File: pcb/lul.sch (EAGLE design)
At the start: 86 parts, among them IC1 STM32F072C8T6, IC2 REG1117, IC3 74AHCT1G08DBV, U1 UG-2864HSWEG01

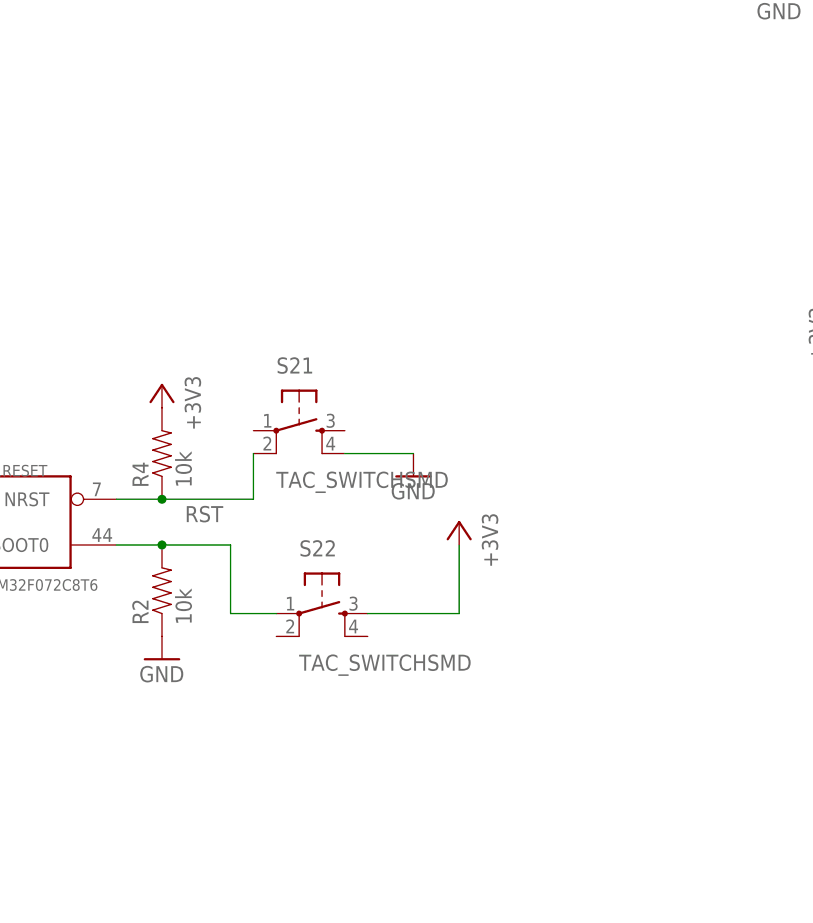
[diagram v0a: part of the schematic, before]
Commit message: replaced DFU and RST button
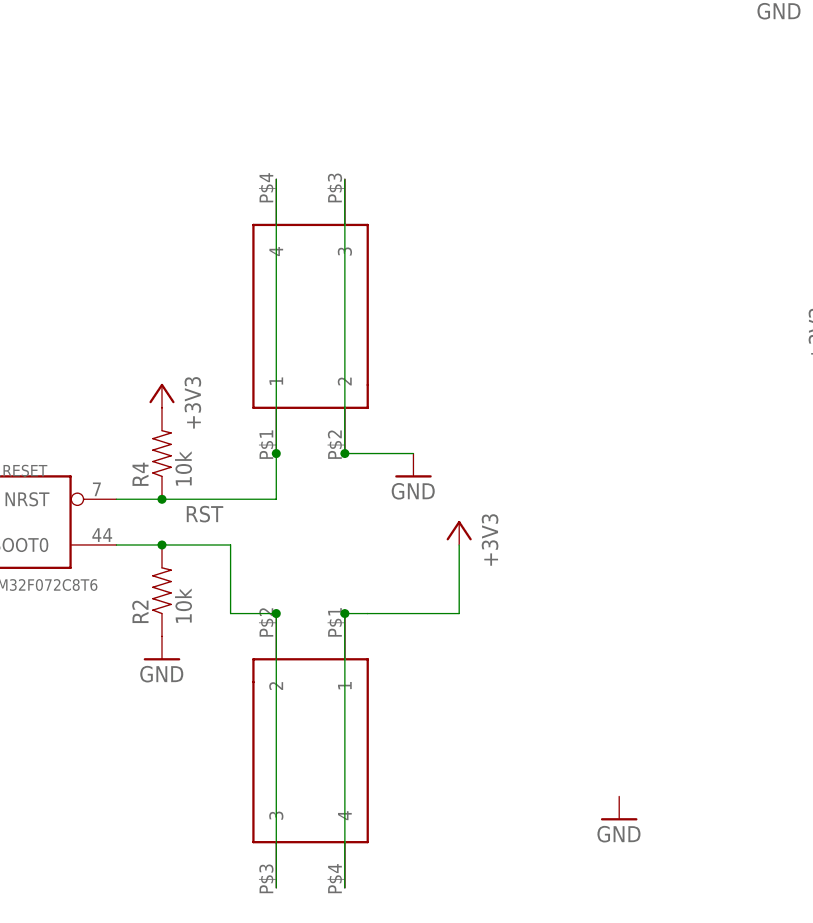
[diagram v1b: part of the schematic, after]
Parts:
- removed S21, S22: TAC_SWITCHSMD, clock:TAC_SWITCHSMD
- added SW1, SW2: 324_SW324_SWITCH_FOOT_HOLE, 3pos_slide_switch:324_SW324_SWITCH_FOOT_HOLE
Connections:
- net +3V3: now also SW1.1, SW1.4; no longer S22.3
- net GND: now also SW2.2, SW2.3; no longer S21.4
- net N$2: now also SW1.2, SW1.3; no longer S22.1
- net RST: now also SW2.1, SW2.4; no longer S21.2
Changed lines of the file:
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@@
 <part name="S19" library="clock" deviceset="TAC_SWITCH" device="SMD" value="TAC_SWITCHSMD"/>
 <part name="S20" library="clock" deviceset="TAC_SWITCH" device="SMD" value="TAC_SWITCHSMD"/>
-<part name="S21" library="clock" deviceset="TAC_SWITCH" device="SMD" value="TAC_SWITCHSMD"/>
-<part name="S22" library="clock" deviceset="TAC_SWITCH" device="SMD" value="TAC_SWITCHSMD"/>
 <part name="IC2" library="clock" deviceset="REG1117" device=""/>
 <part name="+3V3" library="supply1" library_urn="urn:adsk.eagle:library:371" deviceset="+3V3" device=""/>
@@
 <part name="C26" library="clock" deviceset="C-US" device="C1210" value="47uF"/>
 <part name="GND5" library="supply1" library_urn="urn:adsk.eagle:library:371" deviceset="GND" device=""/>
+<part name="GND8" library="supply1" library_urn="urn:adsk.eagle:library:371" deviceset="GND" device=""/>
+<part name="SW2" library="3pos_slide_switch" deviceset="324_SW" device="324_SWITCH_FOOT_HOLE" value="324_SW324_SWITCH_FOOT_HOLE"/>
+<part name="SW1" library="3pos_slide_switch" deviceset="324_SW" device="324_SWITCH_FOOT_HOLE" value="324_SW324_SWITCH_FOOT_HOLE"/>
 </parts>
 <sheets>
@@
 <instance part="S19" gate="S" x="144.78" y="-170.18"/>
 <instance part="S20" gate="S" x="144.78" y="-193.04"/>
-<instance part="S21" gate="S" x="241.3" y="-170.18"/>
-<instance part="S22" gate="S" x="243.84" y="-190.5"/>
 <instance part="IC2" gate="G$1" x="109.22" y="-144.78"/>
 <instance part="+3V3" gate="G$1" x="353.06" y="76.2"/>
@@
 <instance part="C26" gate="G$1" x="86.36" y="-147.32"/>
 <instance part="GND5" gate="1" x="86.36" y="-154.94"/>
+<instance part="GND8" gate="1" x="276.86" y="-213.36"/>
+<instance part="SW2" gate="G$1" x="241.3" y="-157.48" rot="MR90"/>
+<instance part="SW1" gate="G$1" x="243.84" y="-205.74" rot="MR270"/>
 </instances>
 <busses>
@@
 <wire x1="337.82" y1="-180.34" x2="322.58" y2="-180.34" width="0.1524" layer="91"/>
 <junction x="322.58" y="-180.34"/>
-</segment>
-<segment>
-<pinref part="S21" gate="S" pin="4"/>
-<pinref part="GND10" gate="1" pin="GND"/>
-<wire x1="246.38" y1="-172.72" x2="254" y2="-172.72" width="0.1524" layer="91"/>
 </segment>
 <segment>
@@
 <pinref part="GND5" gate="1" pin="GND"/>
 </segment>
+<segment>
+<pinref part="SW2" gate="G$1" pin="2"/>
+<pinref part="GND10" gate="1" pin="GND"/>
+<wire x1="246.38" y1="-172.72" x2="254" y2="-172.72" width="0.1524" layer="91"/>
+<pinref part="SW2" gate="G$1" pin="3"/>
+<wire x1="246.38" y1="-142.24" x2="246.38" y2="-172.72" width="0.1524" layer="91"/>
+<junction x="246.38" y="-172.72"/>
+</segment>
 </net>
 <net name="SCL" class="0">
@@
 </segment>
 <segment>
-<pinref part="S22" gate="S" pin="3"/>
 <pinref part="+3V7" gate="G$1" pin="+3V3"/>
 <wire x1="248.92" y1="-190.5" x2="259.08" y2="-190.5" width="0.1524" layer="91"/>
 <wire x1="259.08" y1="-190.5" x2="259.08" y2="-182.88" width="0.1524" layer="91"/>
+<pinref part="SW1" gate="G$1" pin="1"/>
+<wire x1="248.92" y1="-190.5" x2="246.38" y2="-190.5" width="0.1524" layer="91"/>
+<pinref part="SW1" gate="G$1" pin="4"/>
+<wire x1="246.38" y1="-190.5" x2="246.38" y2="-220.98" width="0.1524" layer="91"/>
+<junction x="246.38" y="-190.5"/>
 </segment>
 <segment>
@@
 <wire x1="233.68" y1="-182.88" x2="233.68" y2="-190.5" width="0.1524" layer="91"/>
 <junction x="226.06" y="-182.88"/>
-<pinref part="S22" gate="S" pin="1"/>
 <wire x1="233.68" y1="-190.5" x2="238.76" y2="-190.5" width="0.1524" layer="91"/>
+<pinref part="SW1" gate="G$1" pin="2"/>
+<pinref part="SW1" gate="G$1" pin="3"/>
+<wire x1="238.76" y1="-190.5" x2="238.76" y2="-220.98" width="0.1524" layer="91"/>
+<junction x="238.76" y="-190.5"/>
 </segment>
 </net>
@@
 <pinref part="R4" gate="G$1" pin="1"/>
 <wire x1="220.98" y1="-177.8" x2="226.06" y2="-177.8" width="0.1524" layer="91"/>
-<pinref part="S21" gate="S" pin="2"/>
-<wire x1="226.06" y1="-177.8" x2="236.22" y2="-177.8" width="0.1524" layer="91"/>
-<wire x1="236.22" y1="-177.8" x2="236.22" y2="-172.72" width="0.1524" layer="91"/>
+<wire x1="226.06" y1="-177.8" x2="238.76" y2="-177.8" width="0.1524" layer="91"/>
 <junction x="226.06" y="-177.8"/>
 <label x="228.6" y="-180.34" size="1.778" layer="95"/>
-</segment>
-</net>
+<pinref part="SW2" gate="G$1" pin="1"/>
+<wire x1="238.76" y1="-177.8" x2="238.76" y2="-172.72" width="0.1524" layer="91"/>
+<pinref part="SW2" gate="G$1" pin="4"/>
+<wire x1="238.76" y1="-142.24" x2="238.76" y2="-172.72" width="0.1524" layer="91"/>
+<junction x="238.76" y="-172.72"/>
+</segment>
+</net>

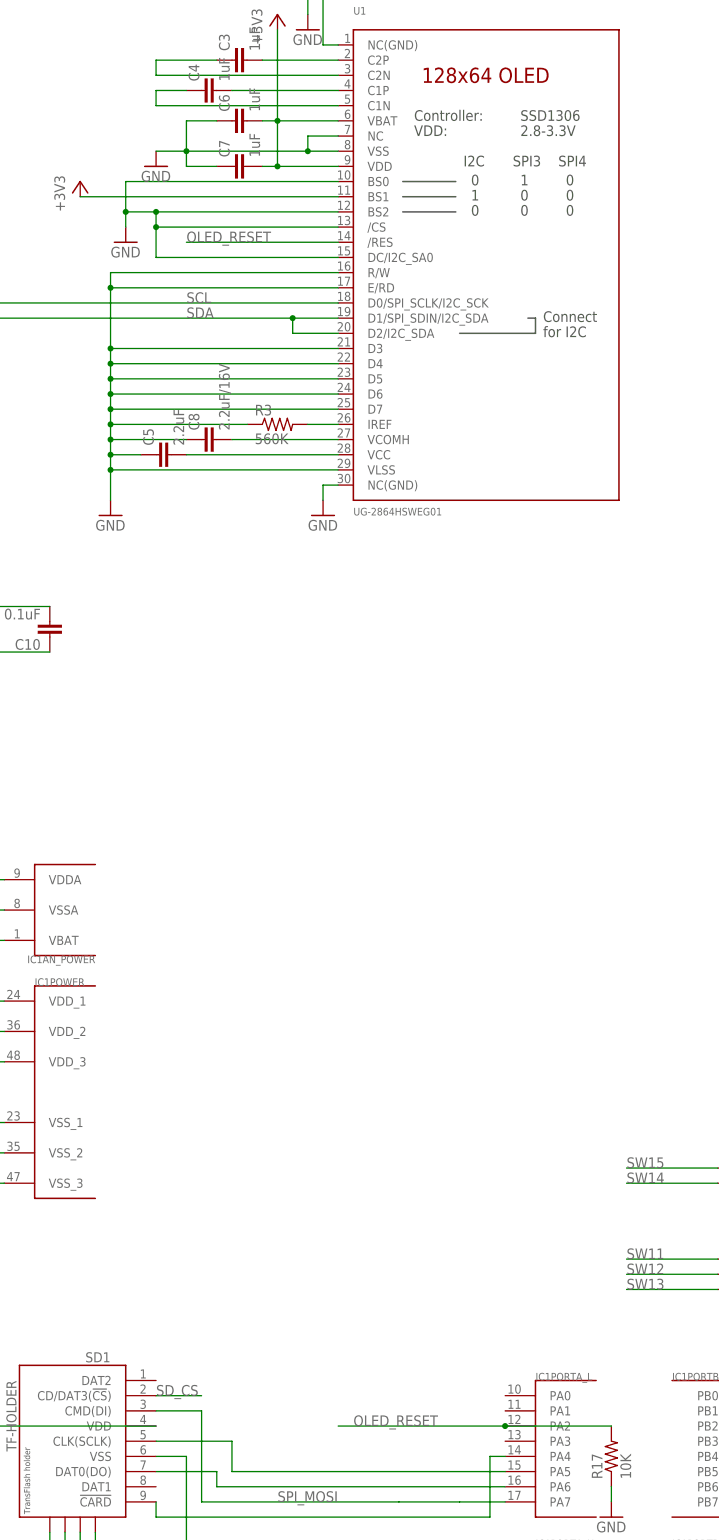
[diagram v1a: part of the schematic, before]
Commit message: new oled socket
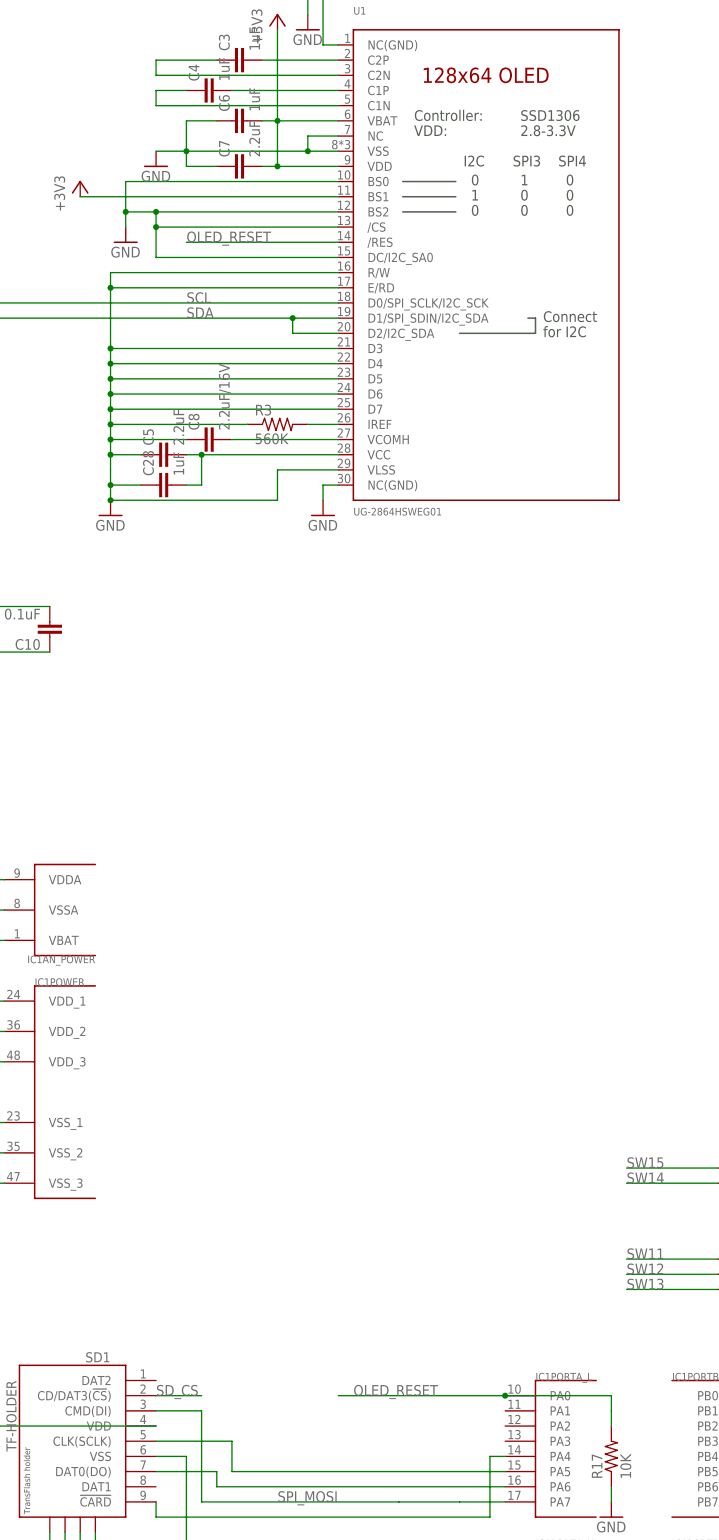
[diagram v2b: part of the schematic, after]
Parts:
- added C28: 1uF, clock:CAP0805
- C7: value 1uF -> 2.2uF
- U1: device lul:DISP_OLED_UG-2864HSWEG010.96" -> lul:LUL_DISP_OLED_UG-2864HSWEG01
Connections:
- net GND: now also C28.1
- net N$11: now also C28.2
- net OLED_RESET: now also IC1PORTA_L.PA0; no longer IC1PORTA_L.PA2
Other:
- moved on the sheet: U1
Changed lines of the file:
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@@
 <part name="S14" library="lul" deviceset="MOMENTARY-SWITCH-SPST-LED" device="-PTH-CHERRY" value="MOMENTARY-SWITCH-SPST-LED-PTH-CHERRY"/>
 <part name="S15" library="lul" deviceset="MOMENTARY-SWITCH-SPST-LED" device="-PTH-CHERRY" value="MOMENTARY-SWITCH-SPST-LED-PTH-CHERRY"/>
-<part name="U1" library="lul" deviceset="DISP_OLED_UG-2864HSWEG01" device="0.96&quot;" value="UG-2864HSWEG01"/>
+<part name="U1" library="lul" deviceset="LUL_DISP_OLED_UG-2864HSWEG01" device="" value="UG-2864HSWEG01"/>
 <part name="U$2" library="supply1" library_urn="urn:adsk.eagle:library:371" deviceset="GND" device=""/>
 <part name="R3" library="clock" deviceset="RESISTOR" device="0805-RES" value="560K"/>
@@
 <part name="C5" library="clock" deviceset="CAP" device="0805" value="2.2uF"/>
 <part name="U$20" library="supply1" library_urn="urn:adsk.eagle:library:371" deviceset="GND" device=""/>
-<part name="C7" library="clock" deviceset="CAP" device="0805" value="1uF"/>
+<part name="C7" library="clock" deviceset="CAP" device="0805" value="2.2uF"/>
 <part name="C8" library="clock" deviceset="CAP" device="0805" value="2.2uF/16V"/>
 <part name="U$21" library="supply1" library_urn="urn:adsk.eagle:library:371" deviceset="GND" device=""/>
@@
 <part name="SW2" library="3pos_slide_switch" deviceset="324_SW" device="324_SWITCH_FOOT_HOLE" value="324_SW324_SWITCH_FOOT_HOLE"/>
 <part name="SW1" library="3pos_slide_switch" deviceset="324_SW" device="324_SWITCH_FOOT_HOLE" value="324_SW324_SWITCH_FOOT_HOLE"/>
+<part name="C28" library="clock" deviceset="CAP" device="0805" value="1uF"/>
 </parts>
 <sheets>
@@
 <instance part="SW2" gate="G$1" x="241.3" y="-157.48" rot="MR90"/>
 <instance part="SW1" gate="G$1" x="243.84" y="-205.74" rot="MR270"/>
+<instance part="C28" gate="G$1" x="335.28" y="-2.54" rot="R90"/>
 </instances>
 <busses>
@@
 </segment>
 <segment>
-<wire x1="363.22" y1="0" x2="325.12" y2="0" width="0.1524" layer="91"/>
+<wire x1="363.22" y1="0" x2="353.06" y2="0" width="0.1524" layer="91"/>
 <wire x1="325.12" y1="0" x2="325.12" y2="2.54" width="0.1524" layer="91"/>
 <wire x1="325.12" y1="2.54" x2="325.12" y2="5.08" width="0.1524" layer="91"/>
@@
 <wire x1="330.2" y1="2.54" x2="325.12" y2="2.54" width="0.1524" layer="91"/>
 <wire x1="337.82" y1="5.08" x2="325.12" y2="5.08" width="0.1524" layer="91"/>
-<wire x1="325.12" y1="0" x2="325.12" y2="-5.08" width="0.1524" layer="91"/>
+<wire x1="325.12" y1="0" x2="325.12" y2="-2.54" width="0.1524" layer="91"/>
 <junction x="325.12" y="2.54"/>
 <junction x="325.12" y="5.08"/>
-<junction x="325.12" y="0"/>
 <pinref part="U1" gate="G$1" pin="VLSS"/>
 <pinref part="R3" gate="G$1" pin="1"/>
@@
 <pinref part="U$21" gate="1" pin="GND"/>
 <pinref part="U1" gate="G$1" pin="D3"/>
+<wire x1="325.12" y1="-2.54" x2="325.12" y2="-5.08" width="0.1524" layer="91"/>
 <wire x1="363.22" y1="20.32" x2="325.12" y2="20.32" width="0.1524" layer="91"/>
 <wire x1="325.12" y1="20.32" x2="325.12" y2="17.78" width="0.1524" layer="91"/>
@@
 <wire x1="325.12" y1="33.02" x2="325.12" y2="30.48" width="0.1524" layer="91"/>
 <junction x="325.12" y="30.48"/>
+<wire x1="325.12" y1="-5.08" x2="353.06" y2="-5.08" width="0.1524" layer="91"/>
+<junction x="325.12" y="-5.08"/>
+<wire x1="353.06" y1="-5.08" x2="353.06" y2="0" width="0.1524" layer="91"/>
+<pinref part="C28" gate="G$1" pin="1"/>
+<wire x1="330.2" y1="-2.54" x2="325.12" y2="-2.54" width="0.1524" layer="91"/>
+<junction x="325.12" y="-2.54"/>
 </segment>
 <segment>
@@
 <net name="N$11" class="0">
 <segment>
-<wire x1="363.22" y1="2.54" x2="337.82" y2="2.54" width="0.1524" layer="91"/>
+<wire x1="363.22" y1="2.54" x2="340.36" y2="2.54" width="0.1524" layer="91"/>
 <pinref part="U1" gate="G$1" pin="VCC"/>
 <pinref part="C5" gate="G$1" pin="2"/>
+<wire x1="340.36" y1="2.54" x2="337.82" y2="2.54" width="0.1524" layer="91"/>
+<wire x1="340.36" y1="2.54" x2="340.36" y2="-2.54" width="0.1524" layer="91"/>
+<junction x="340.36" y="2.54"/>
+<pinref part="C28" gate="G$1" pin="2"/>
+<wire x1="340.36" y1="-2.54" x2="337.82" y2="-2.54" width="0.1524" layer="91"/>
 </segment>
 </net>
@@
 <net name="OLED_RESET" class="0">
 <segment>
-<pinref part="IC1" gate="PORTA_L" pin="PA2"/>
-<wire x1="363.22" y1="-160.02" x2="391.16" y2="-160.02" width="0.1524" layer="91"/>
-<label x="365.76" y="-160.02" size="1.778" layer="95"/>
+<label x="365.76" y="-154.94" size="1.778" layer="95"/>
+<pinref part="IC1" gate="PORTA_L" pin="PA0"/>
+<wire x1="363.22" y1="-154.94" x2="391.16" y2="-154.94" width="0.1524" layer="91"/>
 <pinref part="R17" gate="G$1" pin="2"/>
-<wire x1="391.16" y1="-160.02" x2="408.94" y2="-160.02" width="0.1524" layer="91"/>
-<junction x="391.16" y="-160.02"/>
-</segment>
-<segment>
+<wire x1="408.94" y1="-160.02" x2="408.94" y2="-157.48" width="0.1524" layer="91"/>
+<wire x1="408.94" y1="-157.48" x2="408.94" y2="-154.94" width="0.1524" layer="91"/>
+<wire x1="408.94" y1="-154.94" x2="391.16" y2="-154.94" width="0.1524" layer="91"/>
+<junction x="391.16" y="-154.94"/>
+</segment>
+<segment>
